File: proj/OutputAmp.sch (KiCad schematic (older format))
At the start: 37 parts, among them Q4 MMBT3906, Q5 2N7002, Q6 2N7002, U6 AD8000YRDZ, U7 THS3001IDGN, U8 MAADSS0008

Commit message: Clean up resistor BOM
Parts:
- removed R36: 10k, IPC7351-Nominal:RESC1005X40, symbol R-0402
- removed R37, R40: 1k, IPC7351-Nominal:RESC1005X40, symbol R-0402
- added C54: DNP, IPC7351-Nominal:CAPC1005X55, symbol C-0402
- added R5: 10k, IPC7351-Nominal:RESCAXE80P160X320X70-8, symbol RESPACK-4X0603-CONV
- added R89: DNP, IPC7351-Nominal:RESC1005X40, symbol R-0402
- R35: value 1k -> 1k6; BOM RES SMD 1k 5% [0402] -> RES SMD 1.6k 5% [0402]
- R38, R39: value 220 -> 200; BOM RES SMD 220 5% [0402] -> RES SMD 200 5% [0402]
- R41: value 36 -> 30; BOM RES SMD 36 1% [0402] -> RES SMD 30 1% [0402]
- R43: value 180 -> 150; BOM RES SMD 180 1% [0402] -> RES SMD 150 1% [0402]
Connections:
- net -5: now also R5.1
- net GND: now also C54.2, R5.6, R5.7
- net at R41.1, R43.2, U6.2: now also R89.1
- net at Q5.3, Q6.1, R38.2: now also R5.2
- net at Q6.3, R39.2: now also R5.3
- net at Q4.3, Q5.1: now also R5.8
- new net: C54.1, R89.2
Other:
- moved on the sheet: R41
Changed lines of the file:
@@
 P 6600 1600
 F 0 "R43" V 6400 1600 50  0000 C CNN
-F 1 "180" V 6500 1600 50  0000 C CNN
+F 1 "150" V 6500 1600 50  0000 C CNN
 F 2 "IPC7351-Nominal:RESC1005X40" H 6600 1600 50  0001 C CNN
 F 3 "" H 6600 1650 60  0000 C CNN
 F 4 "Value" H 6600 1600 60  0001 C CNN "Manuf"
-F 5 "RES SMD 180 1% [0402]" H 7350 2150 60  0001 C CNN "BOM"
+F 5 "RES SMD 150 1% [0402]" H 7350 2150 60  0001 C CNN "BOM"
 	1    6600 1600
 	0    1    1    0
@@
 L R-0402 R41
 U 1 1 54F23A28
-P 6200 1600
-F 0 "R41" V 6000 1600 50  0000 C CNN
-F 1 "36" V 6100 1600 50  0000 C CNN
-F 2 "IPC7351-Nominal:RESC1005X40" H 6200 1600 50  0001 C CNN
-F 3 "" H 6200 1650 60  0000 C CNN
-F 4 "Value" H 6200 1600 60  0001 C CNN "Manuf"
-F 5 "RES SMD 36 1% [0402]" H 6950 2150 60  0001 C CNN "BOM"
-	1    6200 1600
+P 6100 1600
+F 0 "R41" V 5900 1600 50  0000 C CNN
+F 1 "30" V 6000 1600 50  0000 C CNN
+F 2 "IPC7351-Nominal:RESC1005X40" H 6100 1600 50  0001 C CNN
+F 3 "" H 6100 1650 60  0000 C CNN
+F 4 "Value" H 6100 1600 60  0001 C CNN "Manuf"
+F 5 "RES SMD 30 1% [0402]" H 6850 2150 60  0001 C CNN "BOM"
+	1    6100 1600
 	0    1    1    0
 $EndComp
 Wire Wire Line
-	6300 1600 6500 1600
+	6200 1600 6500 1600
 Wire Wire Line
 	6400 1600 6400 1800
@@
 L GND #PWR0112
 U 1 1 54F23A9C
-P 6000 1600
-F 0 "#PWR0112" H 6000 1600 30  0001 C CNN
-F 1 "GND" H 6000 1530 30  0001 C CNN
-F 2 "" H 6000 1600 60  0000 C CNN
-F 3 "" H 6000 1600 60  0000 C CNN
-	1    6000 1600
+P 5900 1600
+F 0 "#PWR0112" H 5900 1600 30  0001 C CNN
+F 1 "GND" H 5900 1530 30  0001 C CNN
+F 2 "" H 5900 1600 60  0000 C CNN
+F 3 "" H 5900 1600 60  0000 C CNN
+	1    5900 1600
 	0    1    1    0
 $EndComp
 Wire Wire Line
-	6000 1600 6100 1600
+	5900 1600 6000 1600
 $Comp
 L R-0402 R42
@@
 P 2500 3500
 F 0 "R38" H 2650 3550 50  0000 C CNN
-F 1 "220" H 2650 3450 50  0000 C CNN
+F 1 "200" H 2650 3450 50  0000 C CNN
 F 2 "IPC7351-Nominal:RESC1005X40" H 2500 3500 50  0001 C CNN
 F 3 "" H 2500 3550 60  0000 C CNN
 F 4 "Value" H 2500 3500 60  0001 C CNN "Manuf"
-F 5 "RES SMD 220 5% [0402]" H 3250 4050 60  0001 C CNN "BOM"
+F 5 "RES SMD 200 5% [0402]" H 3250 4050 60  0001 C CNN "BOM"
 	1    2500 3500
 	-1   0    0    -1
@@
 P 2700 3500
 F 0 "R39" H 2850 3550 50  0000 C CNN
-F 1 "220" H 2850 3450 50  0000 C CNN
+F 1 "200" H 2850 3450 50  0000 C CNN
 F 2 "IPC7351-Nominal:RESC1005X40" H 2700 3500 50  0001 C CNN
 F 3 "" H 2700 3550 60  0000 C CNN
 F 4 "Value" H 2700 3500 60  0001 C CNN "Manuf"
-F 5 "RES SMD 220 5% [0402]" H 3450 4050 60  0001 C CNN "BOM"
+F 5 "RES SMD 200 5% [0402]" H 3450 4050 60  0001 C CNN "BOM"
 	1    2700 3500
-	1    0    0    -1
-$EndComp
-$Comp
-L R-0402 R37
-U 1 1 54F28C65
-P 2200 3500
-F 0 "R37" H 2350 3550 50  0000 C CNN
-F 1 "1k" H 2350 3450 50  0000 C CNN
-F 2 "IPC7351-Nominal:RESC1005X40" H 2200 3500 50  0001 C CNN
-F 3 "" H 2200 3550 60  0000 C CNN
-F 4 "Value" H 2200 3500 60  0001 C CNN "Manuf"
-F 5 "RES SMD 1k 5% [0402]" H 2950 4050 60  0001 C CNN "BOM"
-	1    2200 3500
-	-1   0    0    -1
-$EndComp
-$Comp
-L R-0402 R40
-U 1 1 54F28D7D
-P 3000 3500
-F 0 "R40" H 3150 3550 50  0000 C CNN
-F 1 "1k" H 3150 3450 50  0000 C CNN
-F 2 "IPC7351-Nominal:RESC1005X40" H 3000 3500 50  0001 C CNN
-F 3 "" H 3000 3550 60  0000 C CNN
-F 4 "Value" H 3000 3500 60  0001 C CNN "Manuf"
-F 5 "RES SMD 1k 5% [0402]" H 3750 4050 60  0001 C CNN "BOM"
-	1    3000 3500
 	1    0    0    -1
 $EndComp
@@
 	2200 4350 2200 4300
 $Comp
-L R-0402 R36
-U 1 1 54F2AA4A
-P 1800 4600
-F 0 "R36" H 1950 4650 50  0000 C CNN
-F 1 "10k" H 1950 4550 50  0000 C CNN
-F 2 "IPC7351-Nominal:RESC1005X40" H 1800 4600 50  0001 C CNN
-F 3 "" H 1800 4650 60  0000 C CNN
-F 4 "Value" H 1800 4600 60  0001 C CNN "Manuf"
-F 5 "RES SMD 10k 5% [0402]" H 2550 5150 60  0001 C CNN "BOM"
-	1    1800 4600
-	1    0    0    -1
-$EndComp
-$Comp
 L -5 #PWR0144
 U 1 1 54F2AAA9
@@
 P 1800 3700
 F 0 "R35" H 1950 3750 50  0000 C CNN
-F 1 "1k" H 1950 3650 50  0000 C CNN
+F 1 "1k6" H 1950 3650 50  0000 C CNN
 F 2 "IPC7351-Nominal:RESC1005X40" H 1800 3700 50  0001 C CNN
 F 3 "" H 1800 3750 60  0000 C CNN
 F 4 "Value" H 1800 3700 60  0001 C CNN "Manuf"
-F 5 "RES SMD 1k 5% [0402]" H 2550 4250 60  0001 C CNN "BOM"
+F 5 "RES SMD 1.6k 5% [0402]" H 2550 4250 60  0001 C CNN "BOM"
 	1    1800 3700
 	1    0    0    -1
@@
 Wire Wire Line
 	4200 2550 4200 2500
+$Comp
+L R-0402 R89
+U 1 1 54FD59C1
+P 6100 1300
+F 0 "R89" V 5900 1300 50  0000 C CNN
+F 1 "DNP" V 6000 1300 50  0000 C CNN
+F 2 "IPC7351-Nominal:RESC1005X40" H 6100 1300 50  0001 C CNN
+F 3 "" H 6100 1350 60  0000 C CNN
+F 4 "Value" H 6100 1300 60  0001 C CNN "Manuf"
+F 5 "#RES SMD 30 1% [0402]" H 6850 1850 60  0001 C CNN "BOM"
+	1    6100 1300
+	0    1    1    0
+$EndComp
+Wire Wire Line
+	6200 1300 6300 1300
+Wire Wire Line
+	6300 1300 6300 1600
+Connection ~ 6300 1600
+$Comp
+L C-0402 C54
+U 1 1 54FD5C15
+P 5800 1300
+F 0 "C54" V 5550 1300 50  0000 C CNN
+F 1 "DNP" V 5650 1300 50  0000 C CNN
+F 2 "IPC7351-Nominal:CAPC1005X55" H 5800 1300 50  0001 C CNN
+F 3 "" H 5790 1275 60  0000 C CNN
+F 4 "Value" H 5800 1300 60  0001 C CNN "Manuf"
+F 5 "#CAP MLCC 100pF C0G 50V 5% [0402]" H 6600 1850 60  0001 C CNN "BOM"
+	1    5800 1300
+	0    1    1    0
+$EndComp
+Wire Wire Line
+	5900 1300 6000 1300
+$Comp
+L GND #PWR0147
+U 1 1 54FD5E94
+P 5650 1300
+F 0 "#PWR0147" H 5650 1300 30  0001 C CNN
+F 1 "GND" H 5650 1230 30  0001 C CNN
+F 2 "" H 5650 1300 60  0000 C CNN
+F 3 "" H 5650 1300 60  0000 C CNN
+	1    5650 1300
+	0    1    1    0
+$EndComp
+Wire Wire Line
+	5650 1300 5700 1300
+$Comp
+L RESPACK-4X0603-CONV R5
+U 1 1 54FD4E48
+P 1800 4600
+F 0 "R5" H 1650 4550 50  0000 C CNN
+F 1 "10k" H 1650 4650 50  0000 C CNN
+F 2 "IPC7351-Nominal:RESCAXE80P160X320X70-8" H 1800 4600 50  0001 C CNN
+F 3 "" H 1800 4650 60  0000 C CNN
+F 4 "YC164-JR-0710KL" H 1800 4600 60  0001 C CNN "PN"
+F 5 "Yageo" H 1800 4600 60  0001 C CNN "Manuf"
+F 6 "DIST DIGIKEY YC164J-10KCT-ND" H 1800 4600 60  0001 C CNN "BOM"
+	1    1800 4600
+	-1   0    0    1
+$EndComp
+$Comp
+L RESPACK-4X0603-CONV R5
+U 2 1 54FD4F55
+P 2200 3500
+F 0 "R5" H 2050 3450 50  0000 C CNN
+F 1 "10k" H 2050 3550 50  0000 C CNN
+F 2 "IPC7351-Nominal:RESCAXE80P160X320X70-8" H 2200 3500 50  0001 C CNN
+F 3 "" H 2200 3550 60  0000 C CNN
+F 4 "YC164-JR-0710KL" H 2200 3500 60  0001 C CNN "PN"
+F 5 "Yageo" H 2200 3500 60  0001 C CNN "Manuf"
+F 6 "DIST DIGIKEY YC164J-10KCT-ND" H 2200 3500 60  0001 C CNN "BOM"
+	2    2200 3500
+	1    0    0    1
+$EndComp
+$Comp
+L RESPACK-4X0603-CONV R5
+U 3 1 54FD4FD3
+P 3000 3500
+F 0 "R5" H 2850 3450 50  0000 C CNN
+F 1 "10k" H 2850 3550 50  0000 C CNN
+F 2 "IPC7351-Nominal:RESCAXE80P160X320X70-8" H 3000 3500 50  0001 C CNN
+F 3 "" H 3000 3550 60  0000 C CNN
+F 4 "YC164-JR-0710KL" H 3000 3500 60  0001 C CNN "PN"
+F 5 "Yageo" H 3000 3500 60  0001 C CNN "Manuf"
+F 6 "DIST DIGIKEY YC164J-10KCT-ND" H 3000 3500 60  0001 C CNN "BOM"
+	3    3000 3500
+	-1   0    0    1
+$EndComp
 $EndSCHEMATC

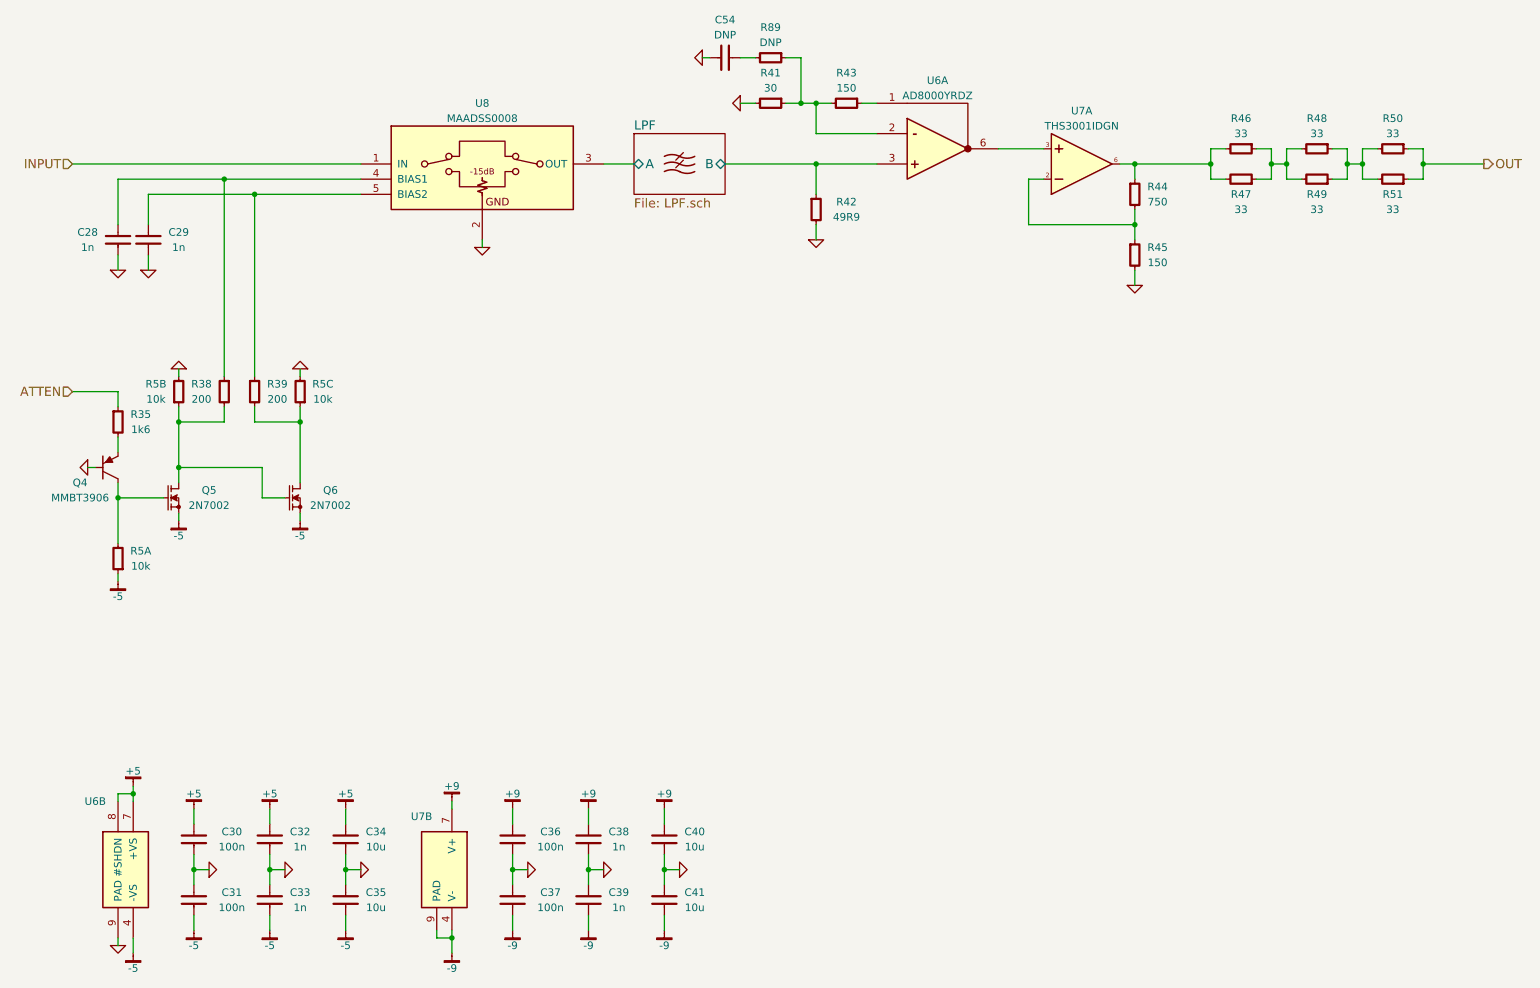
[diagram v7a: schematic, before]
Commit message: Swap 0402 to 0603, add USB inrush protection
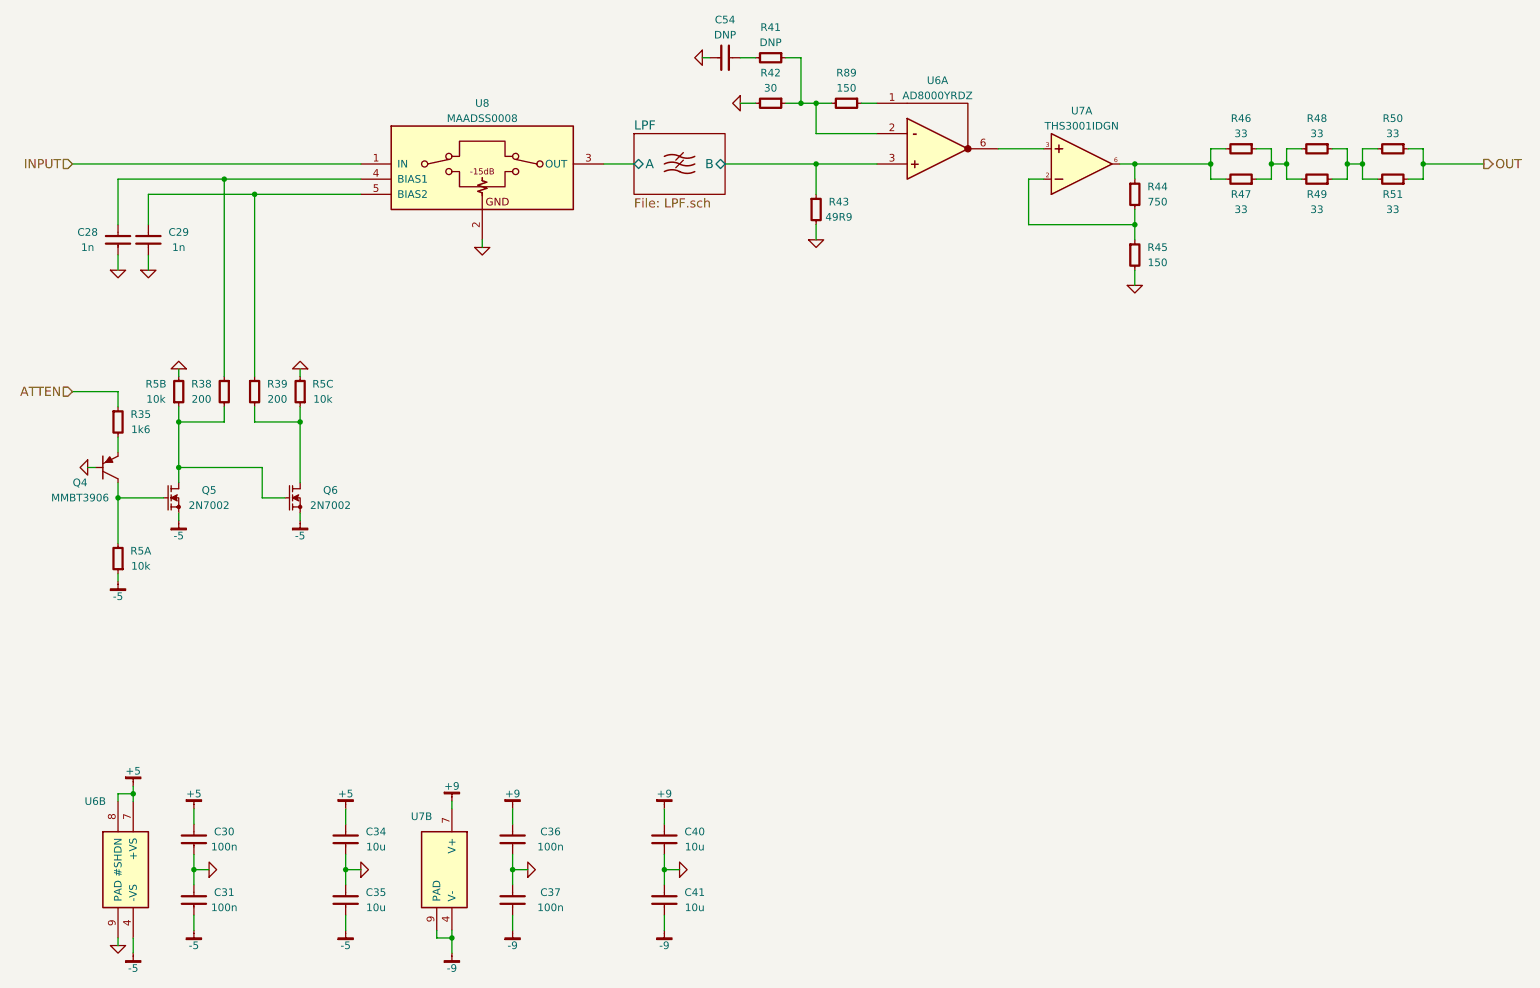
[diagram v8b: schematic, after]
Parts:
- removed C28, C29, C32, C33, C38, C39: 1n, IPC7351-Nominal:CAPC1005X55, symbol C-0402
- removed C30, C31: 100n, IPC7351-Nominal:CAPC2012X70, symbol C-0805
- removed C54: DNP, IPC7351-Nominal:CAPC1005X55, symbol C-0402
- removed R35: 1k6, IPC7351-Nominal:RESC1005X40, symbol R-0402
- removed R38, R39: 200, IPC7351-Nominal:RESC1005X40, symbol R-0402
- removed R41: 30, IPC7351-Nominal:RESC1005X40, symbol R-0402
- removed R42: 49R9, IPC7351-Nominal:RESC1005X40, symbol R-0402
- removed R43, R45: 150, IPC7351-Nominal:RESC1005X40, symbol R-0402
- removed R44: 750, IPC7351-Nominal:RESC1005X40, symbol R-0402
- removed R89: DNP, IPC7351-Nominal:RESC1005X40, symbol R-0402
- added C28, C29: 1n, IPC7351-Nominal:CAPC1608X55, symbol C-0603
- added C30, C31: 100n, IPC7351-Nominal:CAPC1608X55, symbol C-0603
- added C54: DNP, IPC7351-Nominal:CAPC1608X55, symbol C-0603
- added R35: 1k6, IPC7351-Nominal:RESC1608X50, symbol R-0603
- added R38, R39: 200, IPC7351-Nominal:RESC1608X50, symbol R-0603
- added R41: DNP, IPC7351-Nominal:RESC1608X50, symbol R-0603
- added R42: 30, IPC7351-Nominal:RESC1608X50, symbol R-0603
- added R43: 49R9, IPC7351-Nominal:RESC1608X50, symbol R-0603
- added R44: 750, IPC7351-Nominal:RESC1608X50, symbol R-0603
- added R45, R89: 150, IPC7351-Nominal:RESC1608X50, symbol R-0603
- C36, C37: BOM CAP MLCC 100n ≥X5R 16V 10% [0805] -> CAP MLCC 100n ≥X7R 20V 10% [0805]
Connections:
- net +5: now also C30.1
- net -5: now also C31.2
- net ATTEN: now also R35.1
- net GND: now also C28.2, C29.2, C30.2, C31.1, C54.2, R42.2, R43.2, R45.2
- net LPF/B: now also R43.1
- net at U8.4 (BIAS1): now also C28.1, R38.1
- net at U8.5 (BIAS2): now also C29.1, R39.1
- net at U6.1: now also R89.1
- net at U6.2: now also R41.1, R42.1, R89.2
- net at U7.2: now also R44.2, R45.1
- net at R46.2, R47.2, U7.6: now also R44.1
- net at Q5.3, Q6.1, R5.2: now also R38.2
- net at Q6.3, R5.3: now also R39.2
- net at Q4.2: now also R35.2
- new net: C54.1, R41.2
